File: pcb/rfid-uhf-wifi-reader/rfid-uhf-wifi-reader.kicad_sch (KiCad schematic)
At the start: 19 parts, among them J1 USB_OTG, Q1 BSS138, Q2 BSS138, SW1 SW_Push, SW2 SW_Push, U1 ESP32-WROOM-32, U2 AMS1117-3.3, U3 CH340E

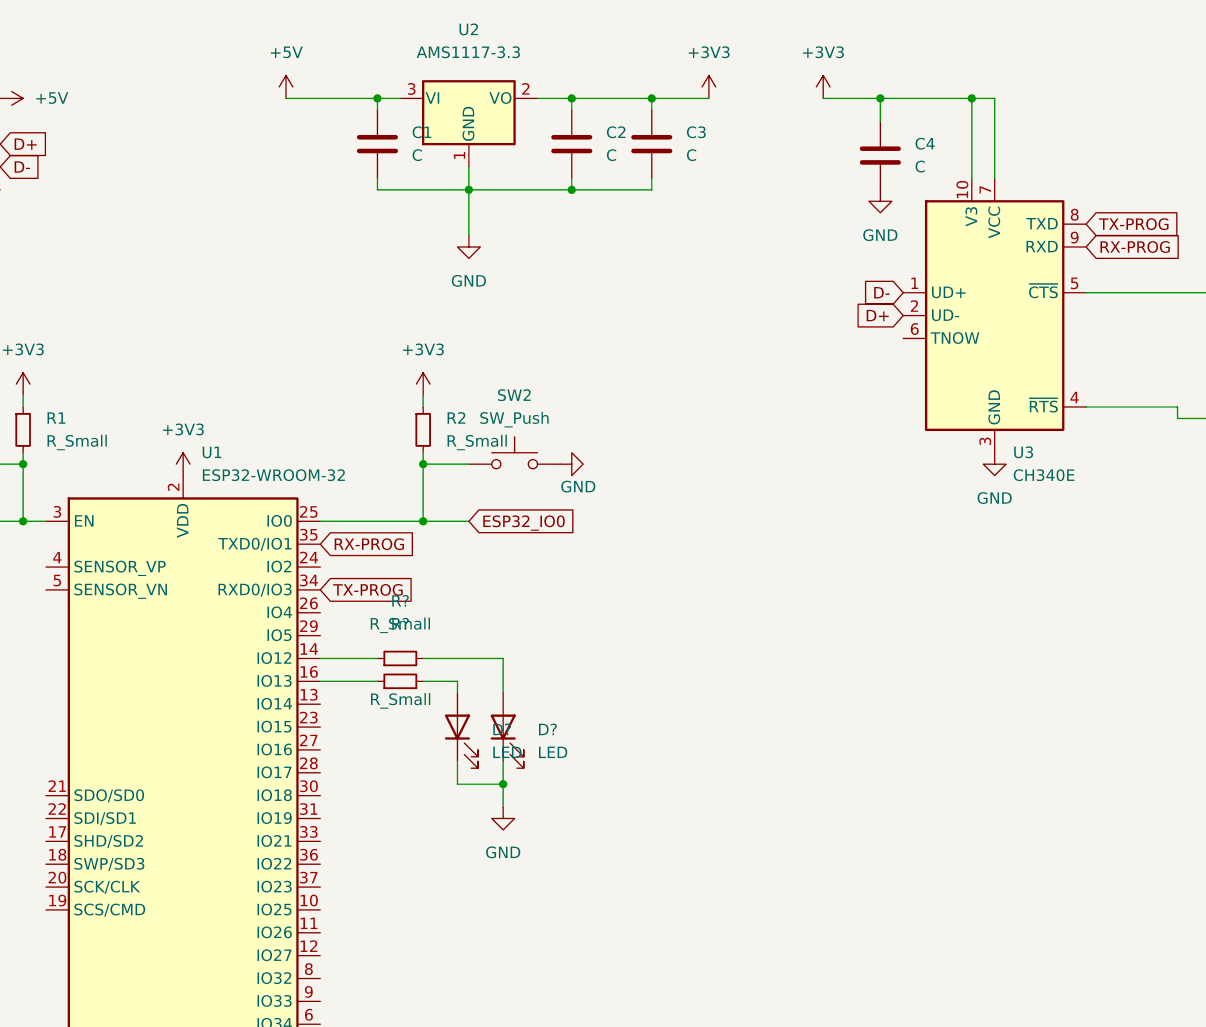
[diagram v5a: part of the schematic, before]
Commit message: add rfid connector
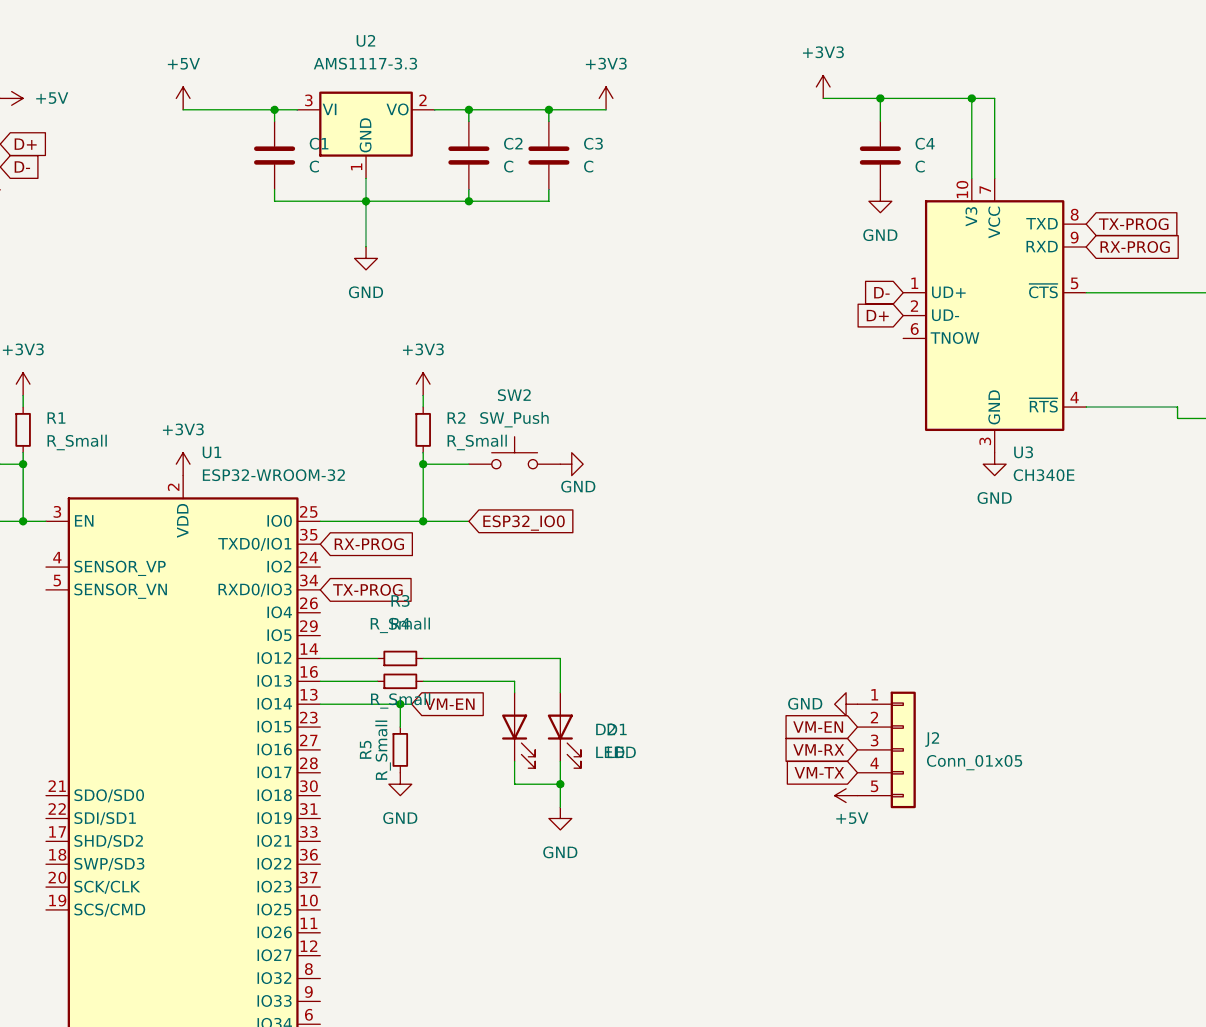
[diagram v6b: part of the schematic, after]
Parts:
- added J2: Conn_01x05, Connector_PinHeader_2.54mm:PinHeader_1x05_P2.54mm_Vertical, symbol Connector_Generic:Conn_01x05
- added R5: R_Small, Resistor_SMD:R_0603_1608Metric, symbol Device:R_Small
- D1, D2: renamed from D?; footprint (none) -> LED_SMD:LED_0603_1608Metric
- gave numbers to parts that had none: 2
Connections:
- net +5V: now also J2.5 (Pin_5)
- net GND: now also J2.1 (Pin_1), R5.2
- net VM-EN: now reaches U1.13 (IO14)
- net VM-EN: now also J2.2 (Pin_2), R5.1
- new net VM-RX: J2.3 (Pin_3)
- new net VM-TX: J2.4 (Pin_4)
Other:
- moved on the sheet: C1, C2, C3, D1, D2, U2

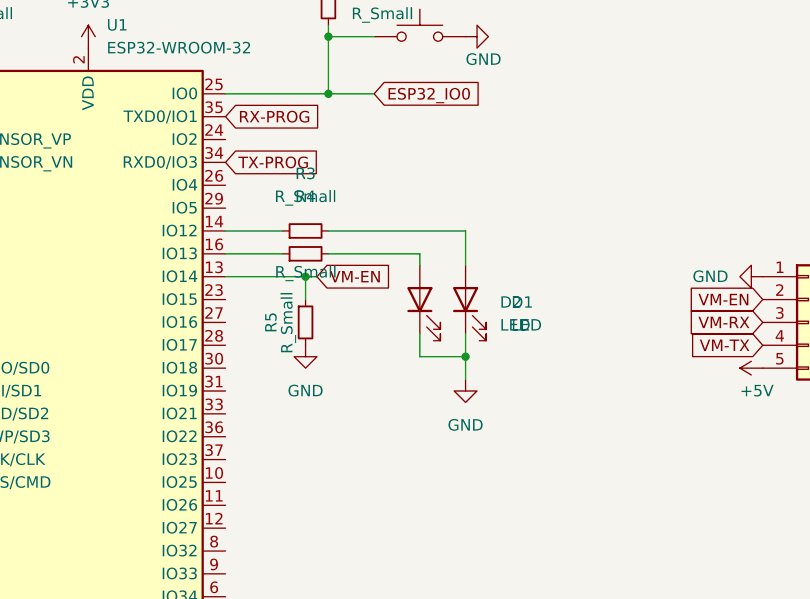
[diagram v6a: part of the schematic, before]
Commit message: add rfid connector
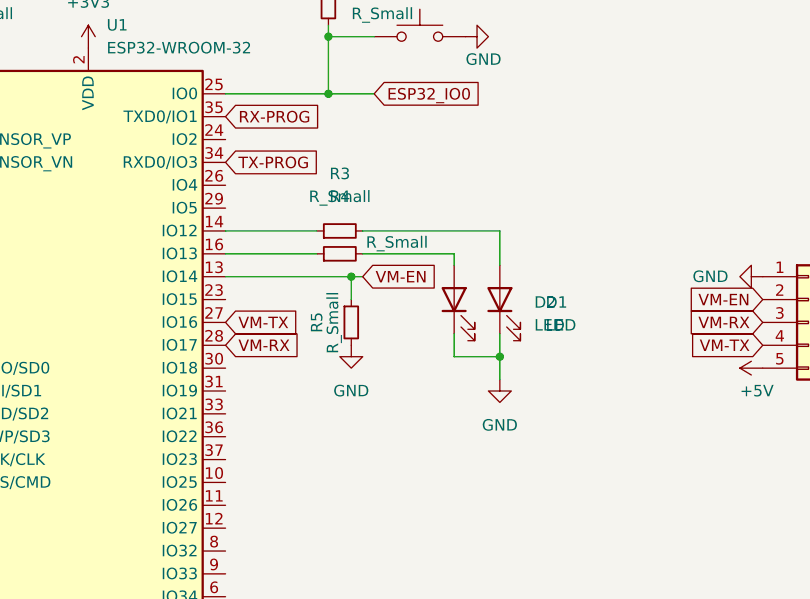
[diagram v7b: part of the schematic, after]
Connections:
- net VM-RX: now also U1.28 (IO17)
- net VM-TX: now also U1.27 (IO16)
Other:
- moved on the sheet: D1, D2, R3, R4, R5

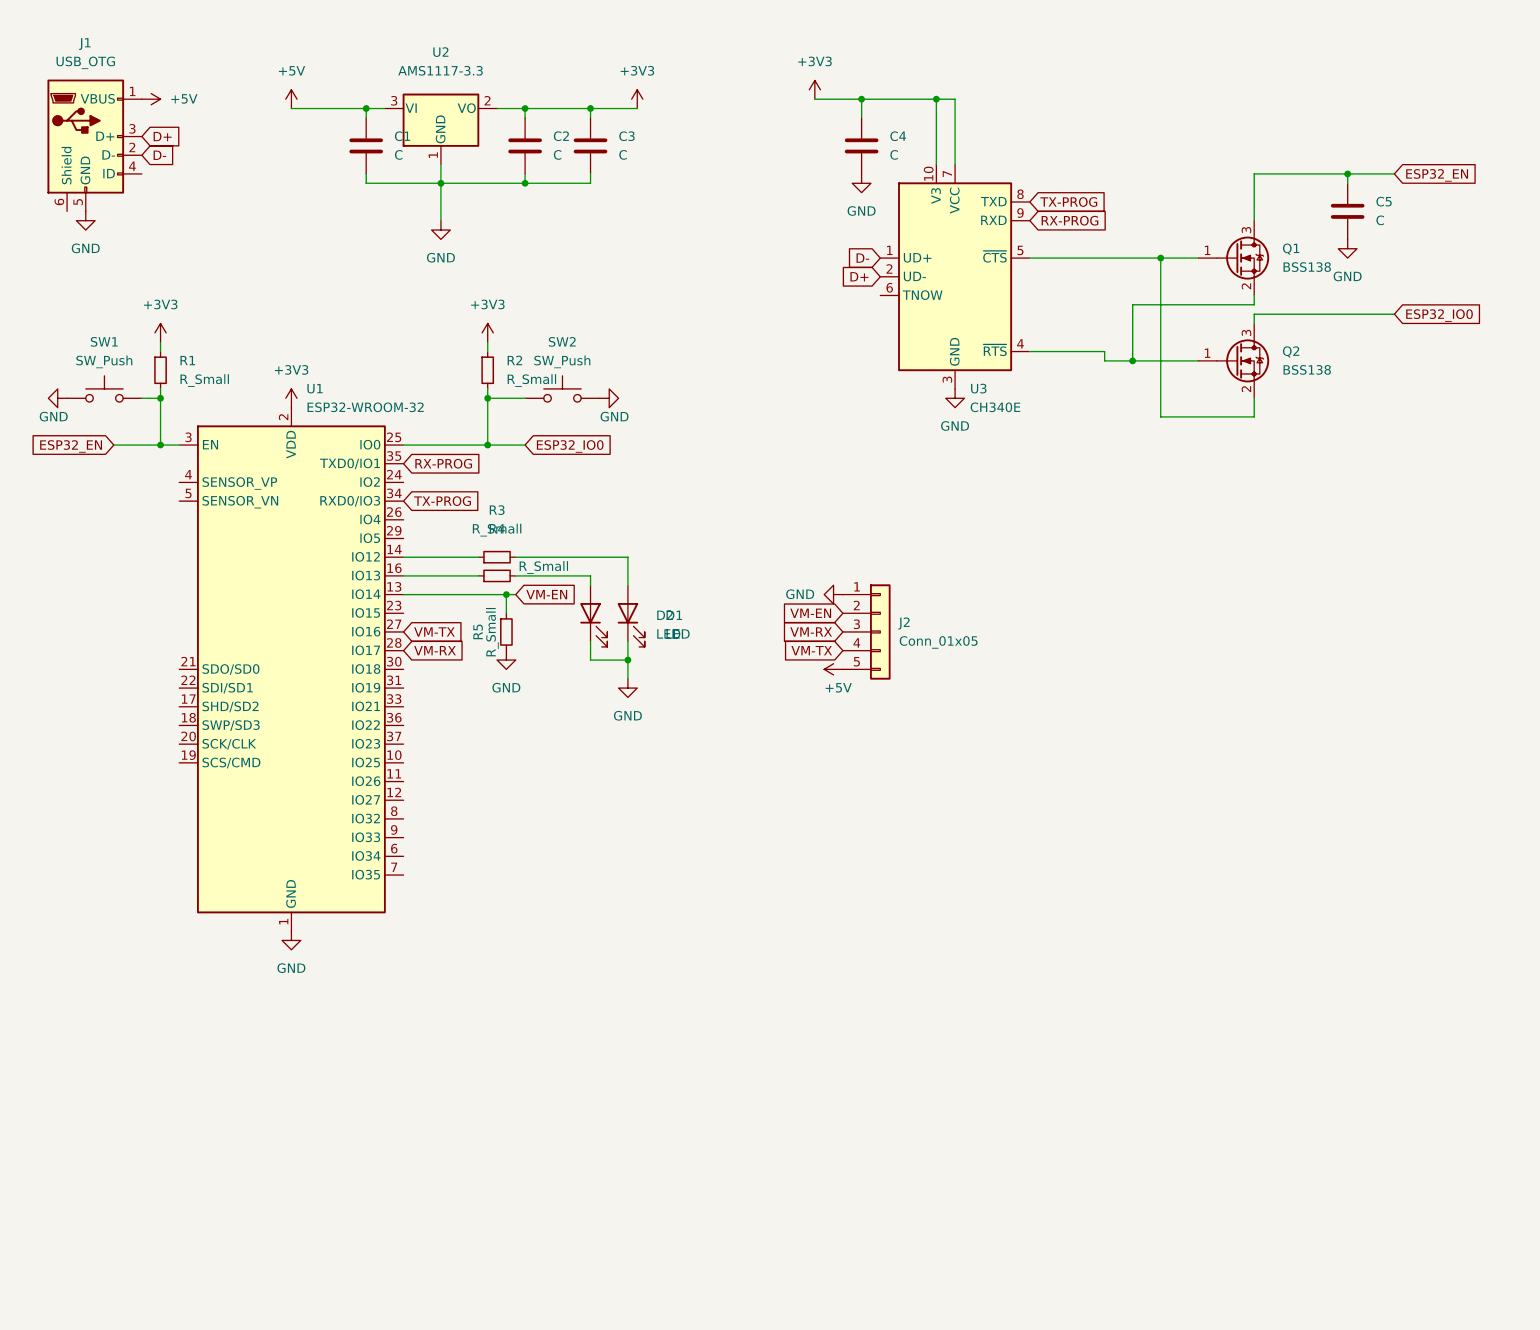
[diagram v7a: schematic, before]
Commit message: add text
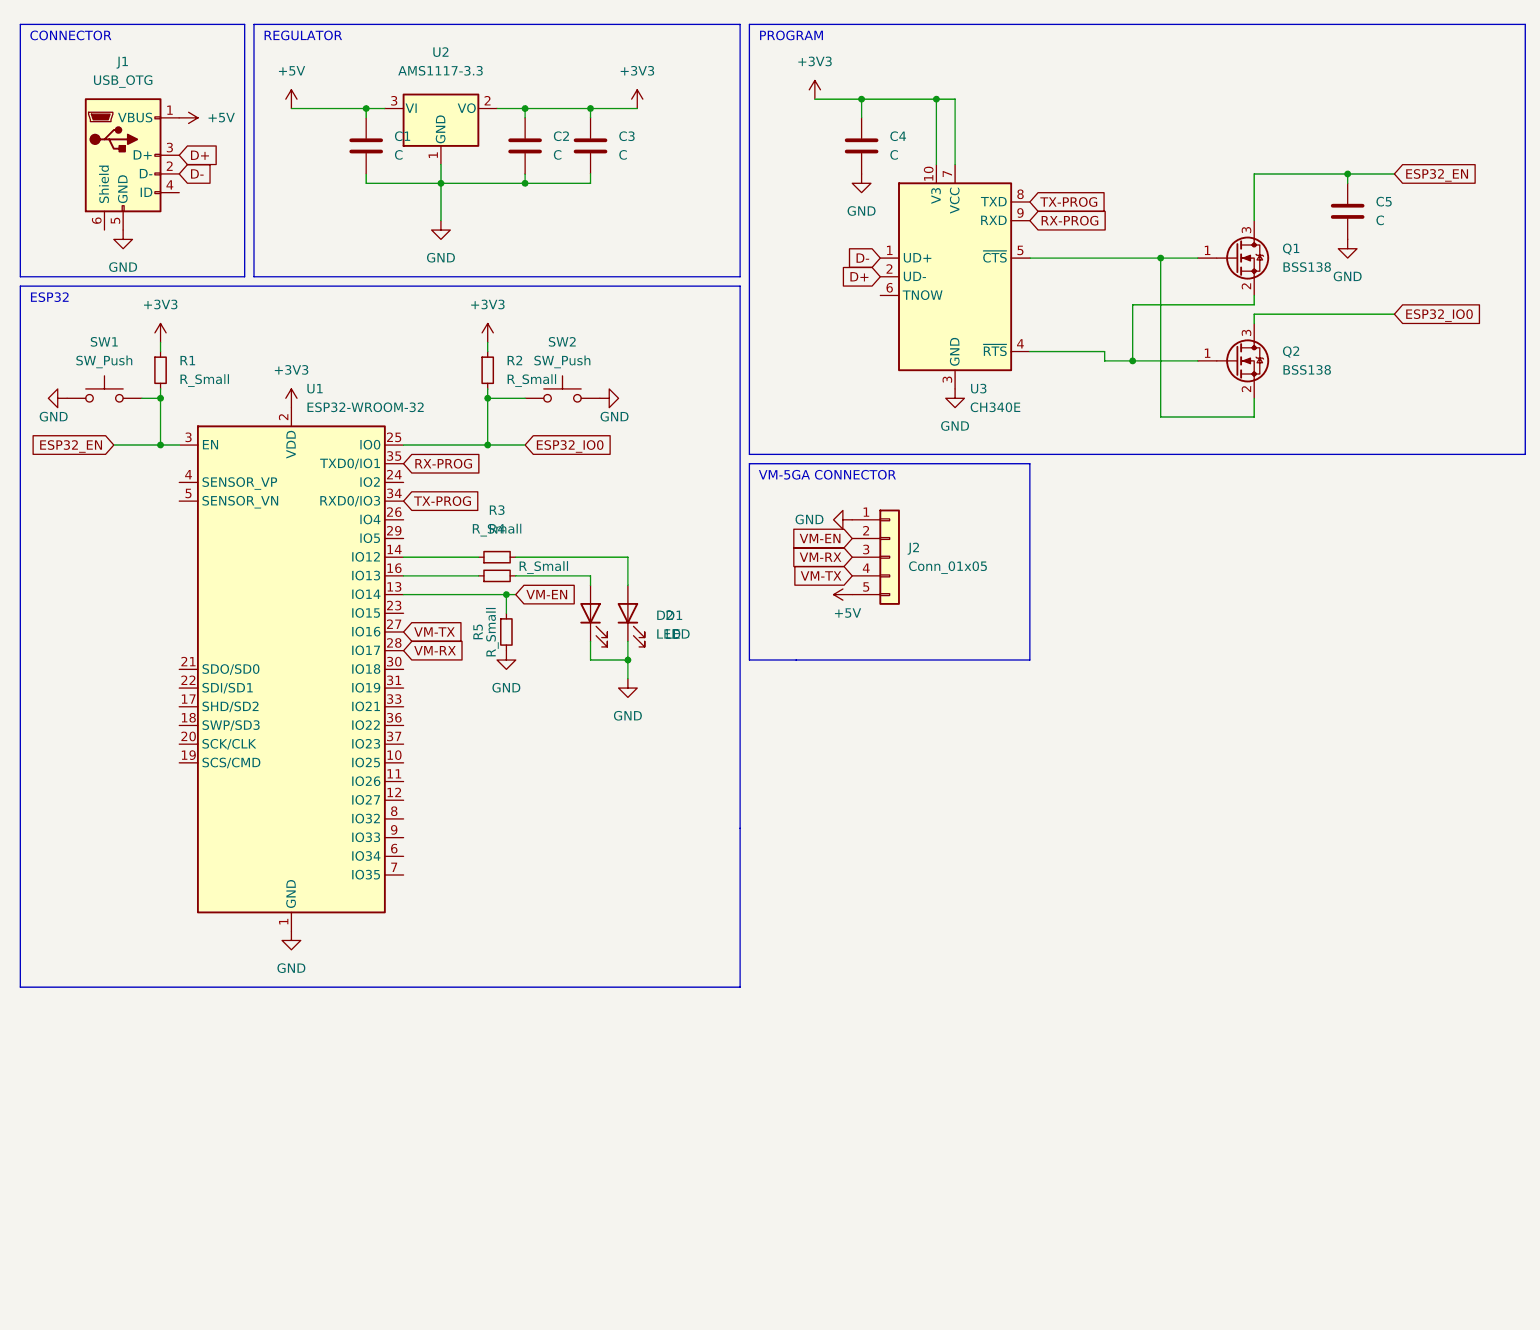
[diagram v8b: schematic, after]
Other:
- note added: "CONNECTOR"
- note added: "ESP32"
- note added: "PROGRAM"
- note added: "REGULATOR"
- note added: "VM-5GA CONNECTOR"
- moved on the sheet: J1, J2
